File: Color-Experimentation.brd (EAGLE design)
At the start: 40.6 x 69.5 mm, 24 parts, among them J1 10118193-0001LF, U2 ATTINY85-20MUR

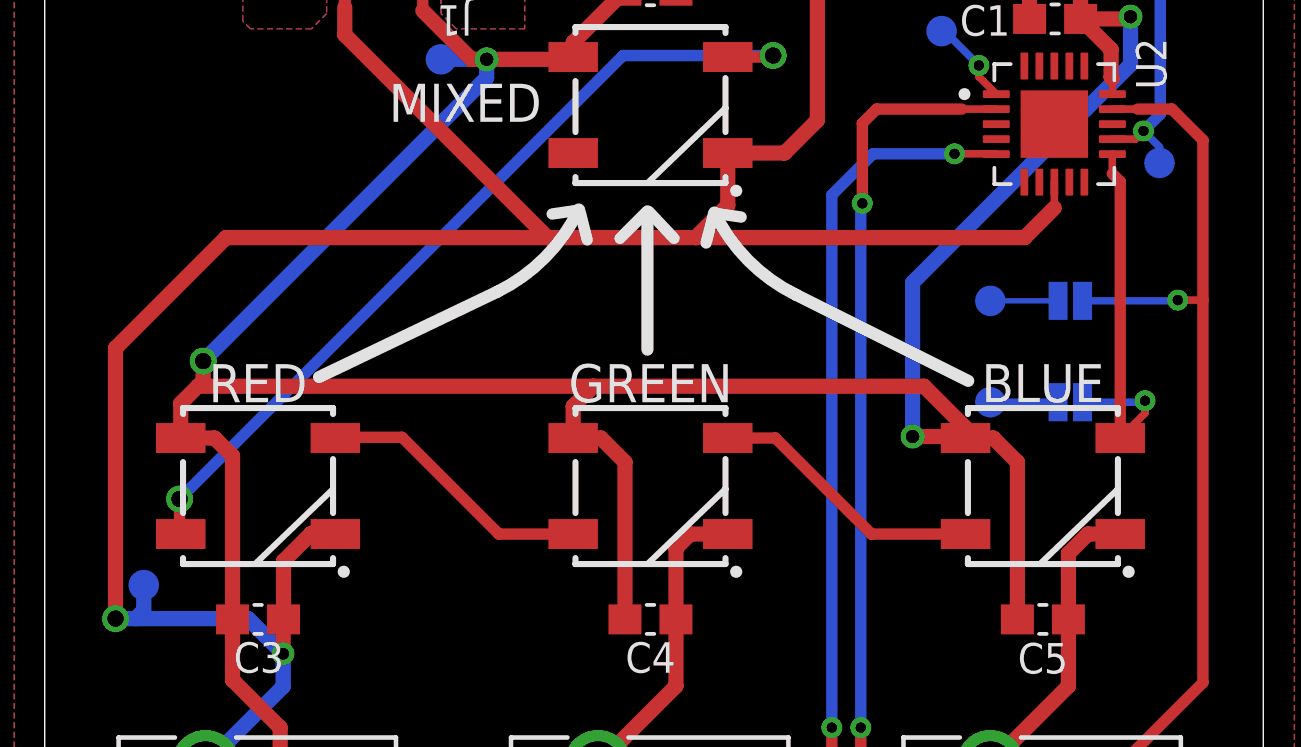
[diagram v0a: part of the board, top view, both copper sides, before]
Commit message: Use LBR, cleanup, export Bill of Materials
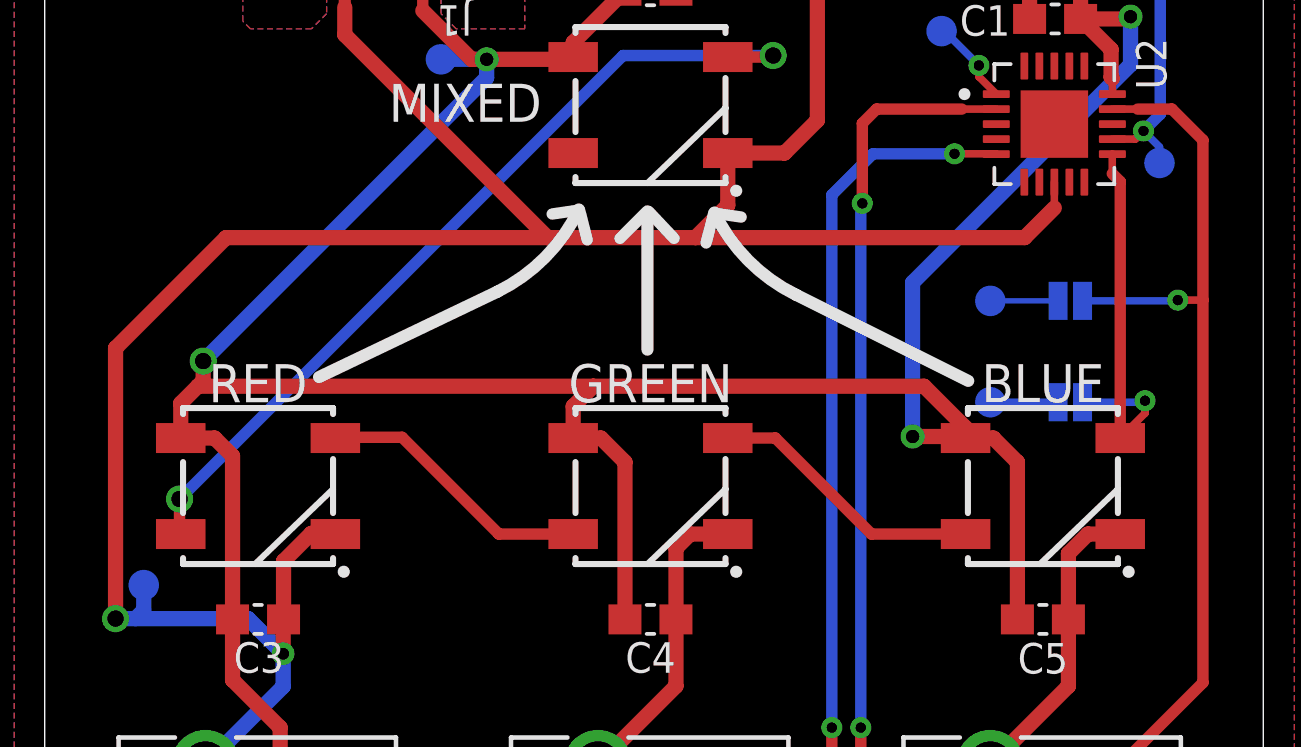
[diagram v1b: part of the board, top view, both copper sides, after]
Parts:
- BLUE, GREEN, MIXED, RED: value WS2812_5050 -> WS2812; device SparkFun-LED:WS2812-5X5-4PIN -> Color-Experimentation:WS2812-5X5-4PIN
- BLUE_POT, GREEN_POT, RED_POT: value PTA2043-2015DPB103 -> 10k; device BoardLE+:POT_PTA2043 -> Color-Experimentation:POT_PTA2043
- C1, C3, C4, C5, C6: device BoardLE+:CAP_0603 -> Color-Experimentation:CAP_0603
- C2: device BoardLE+:C0603 -> Color-Experimentation:C0603
- GND, MISO, MOSI, RST, SCK, VCC: device DoggBone_RC5:TESTPOINT_40MIL_ROUND -> Color-Experimentation:TESTPOINT_40MIL_ROUND
- J1: device BoardLE+:CONN_10118193-0001LF_AMP -> Color-Experimentation:CONN_10118193-0001LF_AMP
- J2: device BoardLE+:1X02 -> Color-Experimentation:1X02
- JP1, JP2: device DoggBone_RC5:SMT-JUMPER_2_NO_SILK -> Color-Experimentation:SMT-JUMPER_2_NO_SILK
- U2: device DoggBone_RC5:QFN-20-THERMAL -> Color-Experimentation:QFN-20-THERMAL

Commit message: Add pullup, solder jumper on "mixed LED enable"
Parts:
- added JP3: JUMPER-SMT_2_NO_SILK, Color-Experimentation:SMT-JUMPER_2_NO_SILK
- added R1: 10k, Color-Experimentation:R0603
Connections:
- new net N$3: J2.2, JP3.1, R1.2
- net N$6: now also JP3.2; no longer J2.2
- net V_USB: now also R1.1
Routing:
- net N$3: track 0.00 -> 25.7 mm
- net N$6: track 25.6 -> 10.8 mm
- net V_USB: track 174.6 -> 175.9 mm
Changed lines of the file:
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@@
 <grid distance="1" unitdist="mil" unit="mil" style="lines" multiple="1" display="yes" altdistance="5" altunitdist="mil" altunit="mil"/>
 <layers>
-<layer number="1" name="Top" color="4" fill="1" visible="no" active="yes"/>
+<layer number="1" name="Top" color="4" fill="1" visible="yes" active="yes"/>
 <layer number="2" name="Route2" color="16" fill="1" visible="no" active="no"/>
 <layer number="3" name="Route3" color="17" fill="1" visible="no" active="no"/>
@@
 <layer number="17" name="Pads" color="2" fill="1" visible="yes" active="yes"/>
 <layer number="18" name="Vias" color="2" fill="1" visible="yes" active="yes"/>
-<layer number="19" name="Unrouted" color="6" fill="1" visible="no" active="yes"/>
+<layer number="19" name="Unrouted" color="6" fill="1" visible="yes" active="yes"/>
 <layer number="20" name="Dimension" color="24" fill="1" visible="yes" active="yes"/>
-<layer number="21" name="tPlace" color="7" fill="1" visible="no" active="yes"/>
-<layer number="22" name="bPlace" color="7" fill="1" visible="no" active="yes"/>
-<layer number="23" name="tOrigins" color="15" fill="1" visible="no" active="yes"/>
-<layer number="24" name="bOrigins" color="15" fill="1" visible="no" active="yes"/>
-<layer number="25" name="tNames" color="7" fill="1" visible="no" active="yes"/>
-<layer number="26" name="bNames" color="7" fill="1" visible="no" active="yes"/>
+<layer number="21" name="tPlace" color="7" fill="1" visible="yes" active="yes"/>
+<layer number="22" name="bPlace" color="7" fill="1" visible="yes" active="yes"/>
+<layer number="23" name="tOrigins" color="15" fill="1" visible="yes" active="yes"/>
+<layer number="24" name="bOrigins" color="15" fill="1" visible="yes" active="yes"/>
+<layer number="25" name="tNames" color="7" fill="1" visible="yes" active="yes"/>
+<layer number="26" name="bNames" color="7" fill="1" visible="yes" active="yes"/>
 <layer number="27" name="tValues" color="7" fill="1" visible="no" active="yes"/>
 <layer number="28" name="bValues" color="7" fill="1" visible="no" active="yes"/>
-<layer number="29" name="tStop" color="7" fill="3" visible="yes" active="yes"/>
+<layer number="29" name="tStop" color="7" fill="3" visible="no" active="yes"/>
 <layer number="30" name="bStop" color="7" fill="6" visible="no" active="yes"/>
 <layer number="31" name="tCream" color="7" fill="4" visible="no" active="yes"/>
@@
 <layer number="37" name="tTest" color="7" fill="1" visible="no" active="yes"/>
 <layer number="38" name="bTest" color="7" fill="1" visible="no" active="yes"/>
-<layer number="39" name="tKeepout" color="4" fill="11" visible="no" active="yes"/>
-<layer number="40" name="bKeepout" color="1" fill="11" visible="no" active="yes"/>
-<layer number="41" name="tRestrict" color="4" fill="10" visible="no" active="yes"/>
-<layer number="42" name="bRestrict" color="1" fill="10" visible="no" active="yes"/>
+<layer number="39" name="tKeepout" color="4" fill="11" visible="yes" active="yes"/>
+<layer number="40" name="bKeepout" color="1" fill="11" visible="yes" active="yes"/>
+<layer number="41" name="tRestrict" color="4" fill="10" visible="yes" active="yes"/>
+<layer number="42" name="bRestrict" color="1" fill="10" visible="yes" active="yes"/>
 <layer number="43" name="vRestrict" color="2" fill="10" visible="no" active="yes"/>
 <layer number="44" name="Drills" color="7" fill="1" visible="no" active="yes"/>
@@
 <layer number="49" name="Reference" color="7" fill="1" visible="no" active="yes"/>
 <layer number="50" name="dxf" color="7" fill="1" visible="no" active="no"/>
-<layer number="51" name="tDocu" color="7" fill="1" visible="no" active="yes"/>
-<layer number="52" name="bDocu" color="7" fill="1" visible="no" active="yes"/>
+<layer number="51" name="tDocu" color="7" fill="1" visible="yes" active="yes"/>
+<layer number="52" name="bDocu" color="7" fill="1" visible="yes" active="yes"/>
 <layer number="53" name="tGND_GNDA" color="7" fill="9" visible="no" active="no"/>
 <layer number="54" name="bGND_GNDA" color="1" fill="9" visible="no" active="no"/>
@@
 <attribute name="VALUE" x="3.302" y="41.656" size="1.016" layer="28" font="vector" ratio="18" rot="MR0" align="top-center"/>
 </element>
+<element name="R1" library="Color-Experimentation" package="R0603" package3d_urn="urn:adsk.eagle:package:23298173/3" value="10k" x="33.655" y="63.881" smashed="yes" rot="R180">
+<attribute name="MFG" value="Yageo" x="33.655" y="63.881" size="1.778" layer="27" rot="R180" display="off"/>
+<attribute name="MPN" value="RC0603FR-0710KL" x="33.655" y="63.881" size="1.778" layer="27" rot="R180" display="off"/>
+<attribute name="NAME" x="31.3436" y="64.4128" size="1.016" layer="25" font="vector" ratio="18" rot="R180" align="bottom-center"/>
+<attribute name="VALUE" x="34.644" y="65.013" size="0.4064" layer="27" rot="R180"/>
+</element>
+<element name="JP3" library="Color-Experimentation" package="SMT-JUMPER_2_NO_SILK" value="JUMPER-SMT_2_NO_SILK" x="34.1884" y="63.246" smashed="yes" rot="MR180">
+<attribute name="VALUE" x="34.1884" y="64.389" size="1.016" layer="28" font="vector" ratio="18" rot="MR180" align="top-center"/>
+</element>
 </elements>
 <signals>
@@
 <wire x1="5.3594" y1="3.175" x2="5.3594" y2="3.5814" width="0.508" layer="16"/>
 <wire x1="17.616" y1="60.02" x2="17.54" y2="59.944" width="0.508" layer="1"/>
+<contactref element="R1" pad="1"/>
+<wire x1="34.505" y1="63.881" x2="34.5304" y2="63.8556" width="0.508" layer="1"/>
+<wire x1="34.5304" y1="63.8556" x2="34.5304" y2="62.5602" width="0.508" layer="1"/>
 </signal>
 <signal name="LED_DATA_OUT">
@@
 <vertex x="6.604" y="67.818"/>
 </polygon>
-<wire x1="14.603" y1="65.548303125" x2="14.605" y2="65.2018" width="0" layer="19" extent="1-1"/>
-<wire x1="14.605" y1="65.8876" x2="14.603" y2="65.548303125" width="0" layer="19" extent="1-1"/>
-<wire x1="8.001" y1="65.2018" x2="8.003" y2="65.548303125" width="0" layer="19" extent="1-1"/>
-<wire x1="8.001" y1="65.8876" x2="8.003" y2="65.548303125" width="0" layer="19" extent="1-1"/>
 </signal>
 <signal name="N$1">
@@
 <via x="36.6268" y="57.5564" extent="1-16" drill="0.35"/>
 <wire x1="37.1602" y1="57.023" x2="36.6268" y2="57.5564" width="0.254" layer="16"/>
-<contactref element="J2" pad="2"/>
-<wire x1="21.463" y1="66.04" x2="34.9504" y2="66.04" width="0.381" layer="16"/>
-<wire x1="34.9504" y1="66.04" x2="37.1856" y2="63.8048" width="0.381" layer="16"/>
-<wire x1="37.1856" y1="63.8048" x2="37.1856" y2="58.1152" width="0.381" layer="16"/>
+<wire x1="37.1856" y1="62.9412" x2="37.1856" y2="58.1152" width="0.381" layer="16"/>
 <wire x1="37.1856" y1="58.1152" x2="36.6268" y2="57.5564" width="0.381" layer="16"/>
 <wire x1="37.1602" y1="56.4896" x2="37.1602" y2="57.023" width="0.254" layer="16"/>
+<contactref element="JP3" pad="2"/>
+<wire x1="34.5948" y1="63.246" x2="36.8808" y2="63.246" width="0.381" layer="16"/>
+<wire x1="36.8808" y1="63.246" x2="37.1856" y2="62.9412" width="0.381" layer="16"/>
+</signal>
+<signal name="N$3">
+<contactref element="J2" pad="2"/>
+<contactref element="R1" pad="2"/>
+<wire x1="32.805" y1="63.881" x2="30.646" y2="66.04" width="0.3048" layer="1"/>
+<wire x1="30.646" y1="66.04" x2="21.463" y2="66.04" width="0.3048" layer="1"/>
+<contactref element="JP3" pad="1"/>
+<wire x1="30.4292" y1="66.04" x2="30.0736" y2="66.04" width="0.381" layer="16"/>
+<wire x1="30.0736" y1="66.04" x2="21.463" y2="66.04" width="0.381" layer="16"/>
+<wire x1="30.4292" y1="66.04" x2="30.988" y2="66.04" width="0.381" layer="16"/>
+<wire x1="30.988" y1="66.04" x2="33.782" y2="63.246" width="0.381" layer="16"/>
 </signal>
 </signals>
@@
 which will not be processed correctly with this version.
 </note>
+<note version="8.3" severity="warning">
+Since Version 8.3, EAGLE supports URNs for individual library
+assets (packages, symbols, and devices). The URNs of those assets
+will not be understood (or retained) with this version.
+</note>
+<note version="8.3" severity="warning">
+Since Version 8.3, EAGLE supports the association of 3D packages
+with devices in libraries, schematics, and board files. Those 3D
+packages will not be understood (or retained) with this version.
+</note>
 </compatibility>

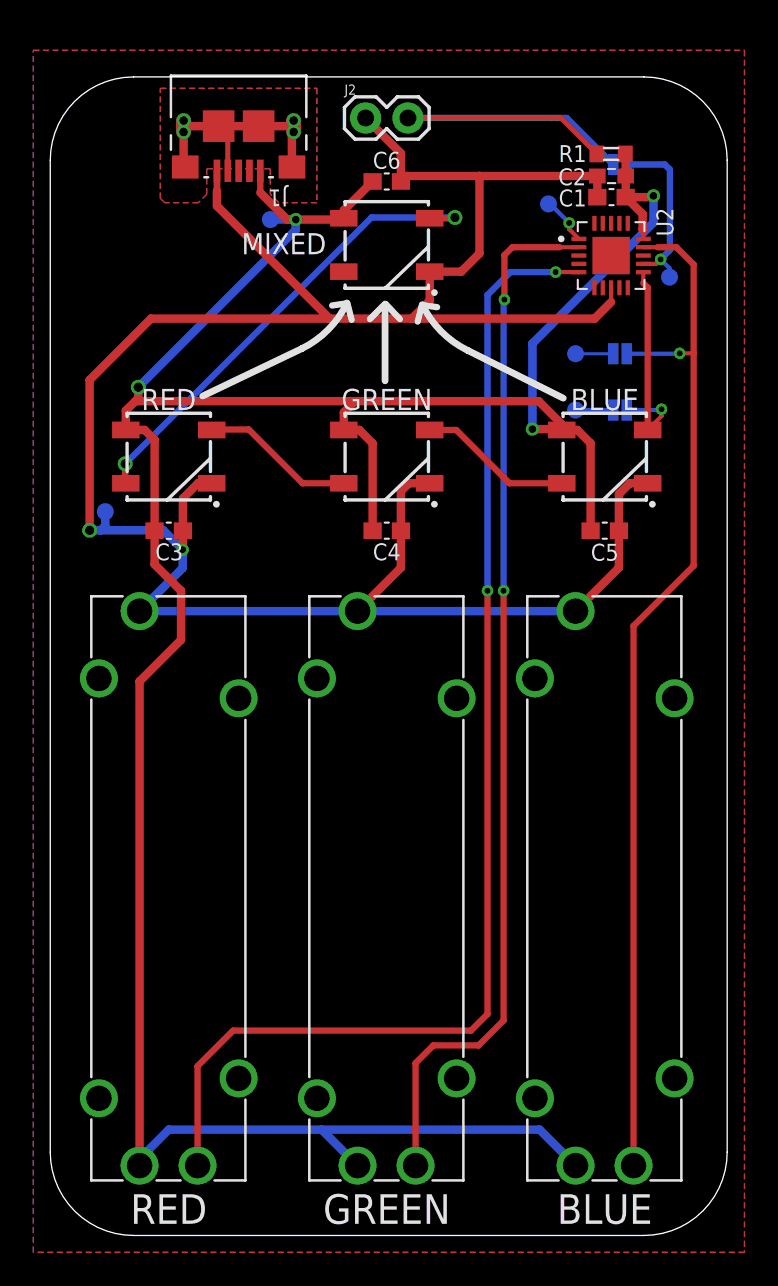
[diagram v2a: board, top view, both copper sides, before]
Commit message: Move corner of board to 0,0
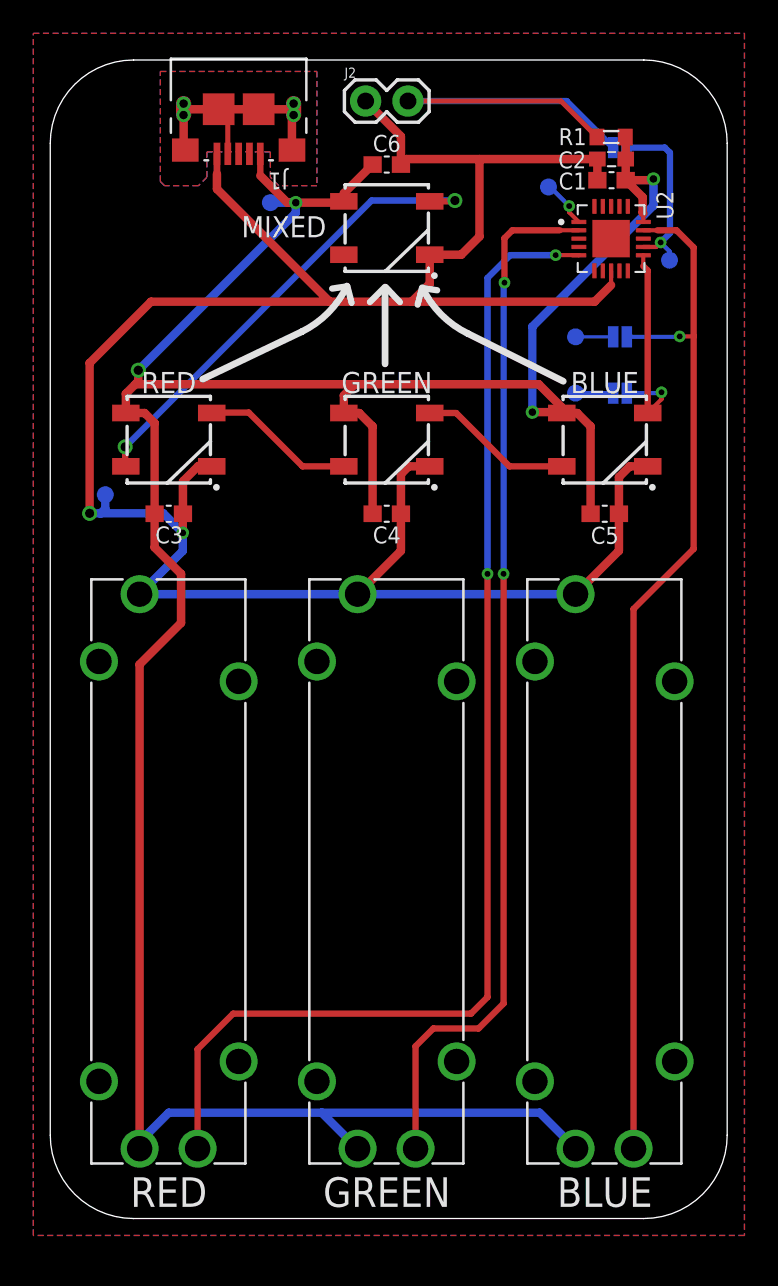
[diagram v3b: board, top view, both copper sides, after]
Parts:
- moved C6 1.02 mm to (20.2, 63.2)
- moved J1 1.02 mm to (11.3, 66.5)
- moved R1 1.02 mm to (33.7, 64.9)
- moved U2 1.02 mm to (33.7, 58.8)
- moved BLUE 1.02 mm to (33.3, 46.7)
- moved BLUE_POT 1.02 mm to (33.3, 20.8)
- moved C1 1.02 mm to (33.7, 62.3)
- moved C2 1.02 mm to (33.7, 63.6)
- moved C3 1.02 mm to (7.11, 42.3)
- moved C4 1.02 mm to (20.2, 42.3)
- moved C5 1.02 mm to (33.3, 42.3)
- moved GND 1.02 mm to (3.30, 43.4)
- moved GREEN 1.02 mm to (20.2, 46.7)
- moved GREEN_POT 1.02 mm to (20.2, 20.8)
- moved JP1 1.02 mm to (34.2, 52.9)
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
